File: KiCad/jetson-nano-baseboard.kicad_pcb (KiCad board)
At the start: 8 copper layers, 100.2 x 55 mm, 325 parts, among them IC1 TCA9548ARGER, IC10 TPS62823DLCT, IC11 SN74LV1T125DCKR, IC12 74HC00PW, IC13 SN74LVC1G126DCKR, IC15 TLV70018DCKT, IC16 NCP380HSNAJAAT1G, IC17 AT24CS01-ST, IC3 TPS54561, IC4 TLV70018DCKT, IC6 PCA9517ADP, IC7 HD3SS3220, IC8 LM3671MF-3.3, IC9 LM3671MF-3.3, J1 685119136923, J11 632723300011, J2 2129320-3, J6 WE_68715014522, J7 WE_68715014022, Q1 PMV32UP, T1 BSS138APW, T2 BSS138APW, T3 BSS138APW, T4 BSS138APW, T5 BSS138APW, T6 BSS138APW

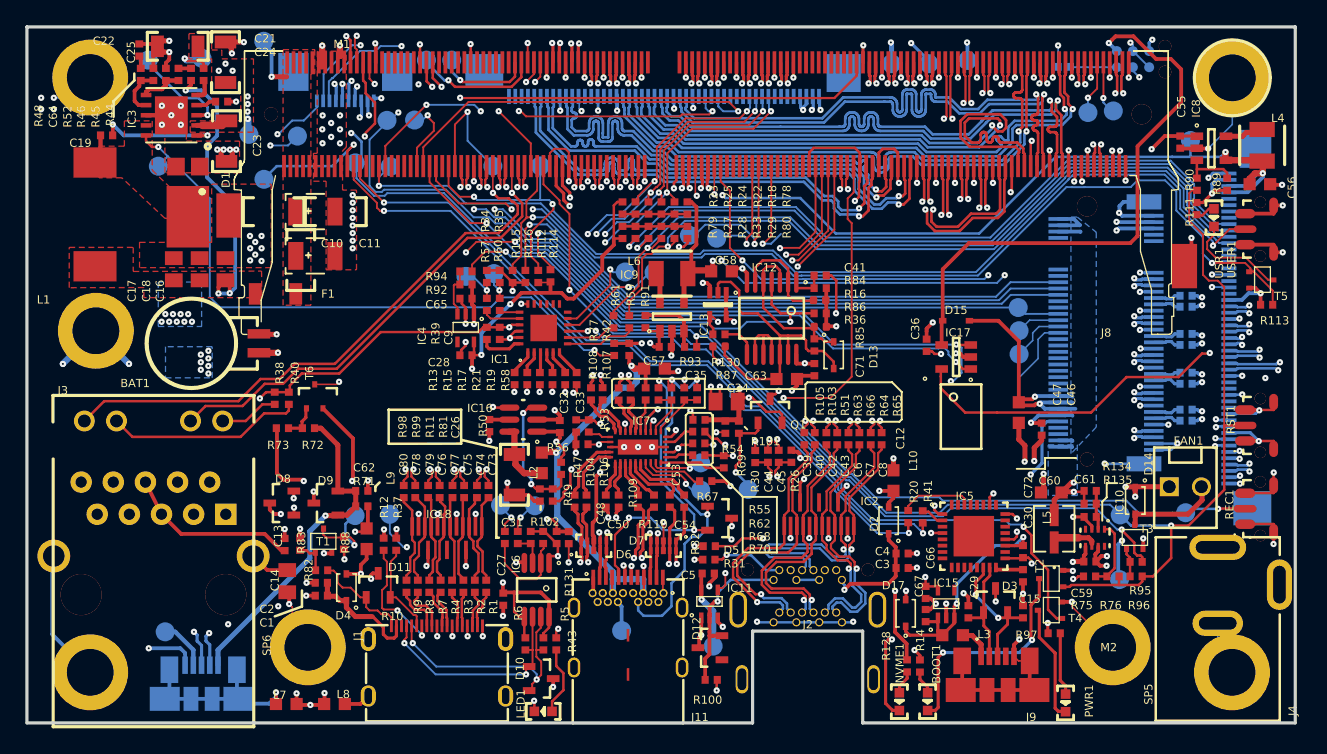
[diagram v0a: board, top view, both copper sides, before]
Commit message: Update 3d models and clean up designators
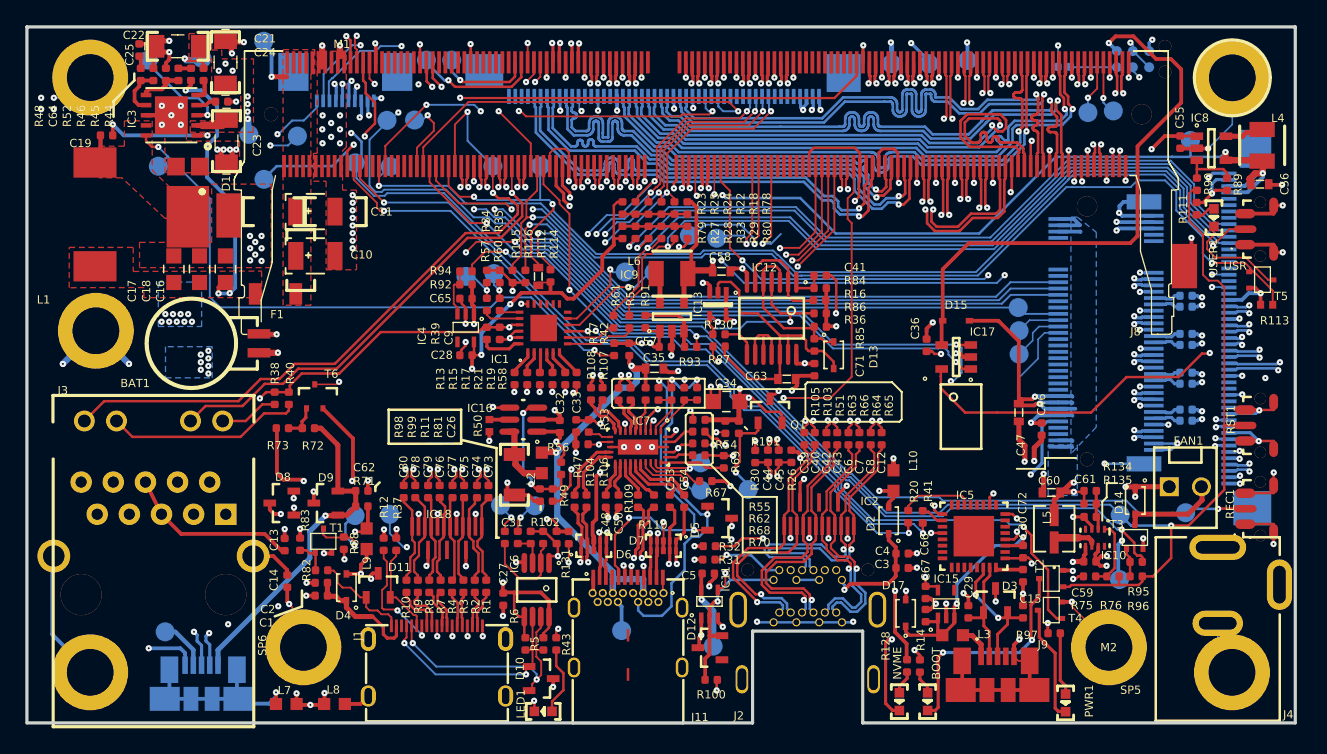
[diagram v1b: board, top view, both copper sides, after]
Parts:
- C1, C2, C3, C4, C62: value 4u7 -> C_4u7_0402; footprint jetson-nano-baseboard-footprints:0402 -> jetson-nano-baseboard-footprints:0402-cap
- C12, C19, C26, C27, C30, C33, C36, C37, C38, C39, C40, C42, C43, C44, C45, C46, C48, C49, C5, C50, C51, C52, C53, C54, C6, C68, C69, C7, C70, C71, C72, C73, C74, C75, C76, C77, C78, C79, C8, C80, C9: value 100n -> C_100n_0402; footprint jetson-nano-baseboard-footprints:0402 -> jetson-nano-baseboard-footprints:0402-cap
- C13, C24: value 10n -> C_10n_0402; footprint jetson-nano-baseboard-footprints:0402 -> jetson-nano-baseboard-footprints:0402-cap
- C14: value 100p -> C_100p_0402; footprint jetson-nano-baseboard-footprints:0805 -> jetson-nano-baseboard-footprints:0402-cap
- C15, C29, C64: value 47p -> C_47p_0402; footprint jetson-nano-baseboard-footprints:0402 -> jetson-nano-baseboard-footprints:0402-cap
- C16, C17, C18, C34: value 47u -> C_47u_0805; footprint jetson-nano-baseboard-footprints:0805 -> jetson-nano-baseboard-footprints:0805-cap
- C21, C22, C23: value 2u2 -> C_2u2_1206; footprint jetson-nano-baseboard-footprints:1206 -> jetson-nano-baseboard-footprints:1206-cap
- C25: value 4n7 -> C_4n7_0402; footprint jetson-nano-baseboard-footprints:0402 -> jetson-nano-baseboard-footprints:0402-cap
- C28, C32, C66: value 1u -> C_1u_0402; footprint jetson-nano-baseboard-footprints:0402 -> jetson-nano-baseboard-footprints:0402-cap
- C35, C47, C56, C58, C60, C63: value 10u -> C_10u_0603; footprint jetson-nano-baseboard-footprints:0603 -> jetson-nano-baseboard-footprints:0603-cap
- C41: value 47n -> C_47n_0402; footprint jetson-nano-baseboard-footprints:0402 -> jetson-nano-baseboard-footprints:0402-cap
- C55, C57: value 4u7 -> C_2u2_0402; footprint jetson-nano-baseboard-footprints:0402 -> jetson-nano-baseboard-footprints:0402-cap
- C59, C65, C67: value 2u2 -> C_2u2_0402; footprint jetson-nano-baseboard-footprints:0402 -> jetson-nano-baseboard-footprints:0402-cap
- C61: value 100p -> C_100p_0402; footprint jetson-nano-baseboard-footprints:0402 -> jetson-nano-baseboard-footprints:0402-cap
- R1, R10, R2, R3, R4, R7, R8, R9: value 5R6 -> R_5R6_0402; footprint jetson-nano-baseboard-footprints:0402 -> jetson-nano-baseboard-footprints:0402-res
- R100, R101, R26, R30, R77: value 100k -> R_100k_0402; footprint jetson-nano-baseboard-footprints:0402 -> jetson-nano-baseboard-footprints:0402-res
- R102, R114, R115, R116, R131, R54, R72, R76, R90, R93, R94, R95, R96: value 10k -> R_10k_0402; footprint jetson-nano-baseboard-footprints:0402 -> jetson-nano-baseboard-footprints:0402-res
- R103, R104, R105, R106, R107, R108, R109, R110, R12, R13, R130, R132, R15, R17, R19, R21, R23, R39, R42, R47, R49, R56, R57, R58, R59, R60, R61, R62, R63, R64, R65, R66, R68, R71, R75, R78, R79, R80, R82, R89, R91, R92, R98, R99: value 0R -> R_0R_0402; footprint jetson-nano-baseboard-footprints:0402 -> jetson-nano-baseboard-footprints:0402-res
- R11, R18, R22, R24, R25, R27, R28, R29, R33, R34, R35, R37, R5, R55, R6, R69, R70, R73, R81, R83, R88: value 2k -> R_2k_0402; footprint jetson-nano-baseboard-footprints:0402 -> jetson-nano-baseboard-footprints:0402-res
- R111, R14, R43, R97: value 470R -> R_470R_0402; footprint jetson-nano-baseboard-footprints:0402 -> jetson-nano-baseboard-footprints:0402-res
- R112: value 100k -> R_110k_0603; footprint jetson-nano-baseboard-footprints:0402 -> jetson-nano-baseboard-footprints:0603-res
- R128, R38, R40: value 220R -> R_220R_0402; footprint jetson-nano-baseboard-footprints:0402 -> jetson-nano-baseboard-footprints:0402-res
- R134, R44: value 243k -> R_243k_0402; footprint jetson-nano-baseboard-footprints:0402 -> jetson-nano-baseboard-footprints:0402-res
- R135, R46: value 53k6 -> R_53k6_0402; footprint jetson-nano-baseboard-footprints:0402 -> jetson-nano-baseboard-footprints:0402-res
- R20, R41: value 22R -> R_22R_0402; footprint jetson-nano-baseboard-footprints:0402 -> jetson-nano-baseboard-footprints:0402-res
- R31, R32: value 1M -> R_1M0_0402; footprint jetson-nano-baseboard-footprints:0402 -> jetson-nano-baseboard-footprints:0402-res
- R45: value 49R9 -> R_49R9_0402; footprint jetson-nano-baseboard-footprints:0402 -> jetson-nano-baseboard-footprints:0402-res
- R48: value 16k9 -> R_16k9_0402; footprint jetson-nano-baseboard-footprints:0402 -> jetson-nano-baseboard-footprints:0402-res
- R51: value 909k -> R_909k_0402; footprint jetson-nano-baseboard-footprints:0402 -> jetson-nano-baseboard-footprints:0402-res
- R52: value 10k2 -> R_10k2_0402; footprint jetson-nano-baseboard-footprints:0402 -> jetson-nano-baseboard-footprints:0402-res
- R53, R67, R84, R86: value 200k -> R_200k_0402; footprint jetson-nano-baseboard-footprints:0402 -> jetson-nano-baseboard-footprints:0402-res
- R85: value 470k -> R_470k_0402; footprint jetson-nano-baseboard-footprints:0402 -> jetson-nano-baseboard-footprints:0402-res
- moved SP6 0.35 mm to (21.8, 48.9)
- moved SP5 0.30 mm to (85.5, 48.9)
- renumbered BOOT1 to BOOT, NVME1 to NVME, USR1 to USR
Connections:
- R50 pad 1: GND -> Net-(R50-Pad1)
- R50 pad 2: Net-(IC16-Pad5) -> Net-(R50-Pad2)
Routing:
- net Net-(R50-Pad1): track 0.00 -> 0.50 mm, vias 0 -> 1
- net GND: track 410.6 -> 410.5 mm, vias 228 -> 227
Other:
- board text removed: "C10"
- board text removed: "C11"
- board text removed: "C12"
- board text removed: "C13"
- board text removed: "C20"
- board text removed: "C22"
- board text removed: "C25"
- board text removed: "C26"
- board text removed: "C27"
- board text removed: "C28"
- board text removed: "C29"
- board text removed: "C30"
- board text removed: "C32"
- board text removed: "C33"
- board text removed: "C34"
- board text removed: "C35"
- board text removed: "C39"
- board text removed: "C40"
- board text removed: "C42"
- board text removed: "C43"
- board text removed: "C44"
- board text removed: "C45"
- board text removed: "C46"
- board text removed: "C47"
- board text removed: "C48"
- board text removed: "C50"
- board text removed: "C53"
- board text removed: "C54"
- board text removed: "C55"
- board text removed: "C56"
- board text removed: "C57"
- board text removed: "C58"
- board text removed: "C6"
- board text removed: "C65"
- board text removed: "C66"
- board text removed: "C67"
- board text removed: "C7"
- board text removed: "C72"
- board text removed: "C73"
- board text removed: "C74"
- board text removed: "C75"
- board text removed: "C76"
- board text removed: "C77"
- board text removed: "C78"
- board text removed: "C79"
- board text removed: "C8"
- board text removed: "C80"
- board text removed: "D1"
- board text removed: "D12"
- board text removed: "D14"
- board text removed: "D2"
- board text removed: "D5"
- board text removed: "F1"
- board text removed: "IC10"
- board text removed: "IC11"
- board text removed: "IC13"
- board text removed: "IC14"
- board text removed: "IC15"
- board text removed: "IC17"
- board text removed: "IC5"
- board text removed: "IC8"
- board text removed: "J9"
- board text removed: "L2"
- board text removed: "L9"
- board text removed: "NVME"
- board text removed: "Q2"
- board text removed: "R1"
- board text removed: "R10"
- board text removed: "R100"
- board text removed: "R103"
- board text removed: "R105"
- board text removed: "R107"
- board text removed: "R108"
- board text removed: "R109"
- board text removed: "R11"
- board text removed: "R111"
- board text removed: "R117"
- board text removed: "R118"
- board text removed: "R119"
- board text removed: "R120"
- board text removed: "R121"
- board text removed: "R122"
- board text removed: "R123"
- board text removed: "R124"
- board text removed: "R125"
- board text removed: "R126"
- board text removed: "R127"
- board text removed: "R129"
- board text removed: "R13"
- board text removed: "R130"
- board text removed: "R131"
- board text removed: "R15"
- board text removed: "R17"
- board text removed: "R18"
- board text removed: "R19"
- board text removed: "R2"
- board text removed: "R21"
- board text removed: "R22"
- board text removed: "R23"
- board text removed: "R24"
- board text removed: "R25"
- board text removed: "R26"
- board text removed: "R27"
- board text removed: "R28"
- board text removed: "R29"
- board text removed: "R3"
- board text removed: "R30"
- board text removed: "R31"
- board text removed: "R32"
- board text removed: "R33"
- board text removed: "R38"
- board text removed: "R4"
- board text removed: "R40"
- board text removed: "R42"
- board text removed: "R43"
- board text removed: "R5"
- board text removed: "R50"
- board text removed: "R51"
- board text removed: "R54"
- board text removed: "R55"
- board text removed: "R58"
- board text removed: "R6"
- board text removed: "R62"
- board text removed: "R63"
- board text removed: "R64"
- board text removed: "R65"
- board text removed: "R66"
- board text removed: "R67"
- board text removed: "R68"
- board text removed: "R69"
- board text removed: "R7"
- board text removed: "R70"
- board text removed: "R74"
- board text removed: "R77"
- board text removed: "R78"
- board text removed: "R79"
- board text removed: "R8"
- board text removed: "R80"
- board text removed: "R81"
- board text removed: "R82"
- board text removed: "R83"
- board text removed: "R87"
- board text removed: "R88"
- board text removed: "R89"
- board text removed: "R9"
- board text removed: "R90"
- board text removed: "R92"
- board text removed: "R94"
- board text removed: "R95"
- board text removed: "R98"
- board text removed: "R99"
- board text removed: "SP5"
- board text removed: "T1"
- board text removed: "T3"
- board text removed: "USER"

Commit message: Fix DRC errors
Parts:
- moved C25 0.29 mm to (8.54, 1.73)
- moved D1 0.13 mm to (12.6, 14.3)
- renumbered BOOT to BOOT1, NVME to NVME1, USR to USR1
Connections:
- R50 pad 1: Net-(R50-Pad1) -> GND
- R50 pad 2: Net-(R50-Pad2) -> Net-(IC16-Pad5)
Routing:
- net GND: track 410.5 -> 411.3 mm, vias 227 -> 228
- net Net-(R50-Pad1): track 0.50 -> 0.00 mm, vias 1 -> 0
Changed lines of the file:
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@@
     (zones 0)
     (modules 325)
-    (nets 441)
+    (nets 439)
   )
   (page A4)
   (layers
     (0 F.Cu signal)
-    (1 In1.Cu signal)
-    (2 In2.Cu signal)
-    (3 In3.Cu signal)
-    (4 In4.Cu signal)
-    (5 In5.Cu signal)
-    (6 In6.Cu signal)
+    (1 In1.Cu signal hide)
+    (2 In2.Cu signal hide)
+    (3 In3.Cu signal hide)
+    (4 In4.Cu signal hide)
+    (5 In5.Cu signal hide)
+    (6 In6.Cu signal hide)
     (31 B.Cu signal)
     (32 B.Adhes user hide)
     (33 F.Adhes user hide)
-    (34 B.Paste user hide)
-    (35 F.Paste user hide)
-    (36 B.SilkS user hide)
-    (37 F.SilkS user hide)
+    (34 B.Paste user)
+    (35 F.Paste user)
+    (36 B.SilkS user)
+    (37 F.SilkS user)
     (38 B.Mask user hide)
     (39 F.Mask user hide)
-    (40 Dwgs.User user)
+    (40 Dwgs.User user hide)
     (41 Cmts.User user hide)
     (42 Eco1.User user hide)
@@
     (45 Margin user hide)
     (46 B.CrtYd user hide)
-    (47 F.CrtYd user hide)
+    (47 F.CrtYd user)
     (48 B.Fab user hide)
     (49 F.Fab user hide)
@@
   (net 437 PWR_GOOD)
   (net 438 "#RECOVERY")
-  (net 439 "Net-(R50-Pad1)")
-  (net 440 "Net-(R50-Pad2)")
   (net_class Default "This is the default net class."
     (clearance 0.1)
@@
     (add_net "Net-(R27-Pad1)")
     (add_net "Net-(R45-Pad1)")
-    (add_net "Net-(R50-Pad1)")
-    (add_net "Net-(R50-Pad2)")
     (add_net "Net-(R72-Pad2)")
     (add_net "Net-(R82-Pad2)")
@@
   )
   (module jetson-nano-baseboard-footprints:0402-res (layer F.Cu)
-    (at 85.7822 43.32361)
+    (at 85.745 43.32)
     (descr "Resistor SMD 0402 (1005 Metric), square (rectangular) end terminal, IPC_7351 nominal, (Body size source: http://www.tortai-tech.com/upload/download/2011102023233369053.pdf), generated with kicad-footprint-generator")
     (tags resistor)
@@
   )
   (module jetson-nano-baseboard-footprints:0402-res (layer F.Cu)
-    (at 83.928 43.32361 180)
+    (at 83.88 43.32 180)
     (descr "Resistor SMD 0402 (1005 Metric), square (rectangular) end terminal, IPC_7351 nominal, (Body size source: http://www.tortai-tech.com/upload/download/2011102023233369053.pdf), generated with kicad-footprint-generator")
     (tags resistor)
@@
   )
   (module jetson-nano-baseboard-footprints:0402-cap (layer F.Cu)
-    (at 8.83927 1.7324 270)
+    (at 8.545 1.725 270)
     (descr "Resistor SMD 0402 (1005 Metric), square (rectangular) end terminal, IPC_7351 nominal, (Body size source: http://www.tortai-tech.com/upload/download/2011102023233369053.pdf), generated with kicad-footprint-generator")
     (tags resistor)
     (attr smd)
-    (fp_text reference C25 (at 0.3676 0.76927 90) (layer F.SilkS)
+    (fp_text reference C25 (at 0.3 0.84 90) (layer F.SilkS)
       (effects (font (size 0.65 0.65) (thickness 0.15)))
     )
@@
     (at 97.424 15.88801)
     (attr smd)
-    (fp_text reference USR (at -1.979 2.89699) (layer F.SilkS)
+    (fp_text reference USR1 (at -1.979 2.89699) (layer F.SilkS)
       (effects (font (size 0.65 0.65) (thickness 0.15)))
     )
@@
     )
     (pad 1 smd rect (at -0.48 0 180) (size 0.62 0.57) (layers F.Cu F.Paste F.Mask)
-      (net 439 "Net-(R50-Pad1)"))
+      (net 6 GND))
     (pad 2 smd rect (at 0.48 0 180) (size 0.62 0.57) (layers F.Cu F.Paste F.Mask)
-      (net 440 "Net-(R50-Pad2)"))
+      (net 84 "Net-(IC16-Pad5)"))
     (model ${KIPRJMOD}/nano-baseboard-3dmodels/0402-res.step
       (at (xyz 0 0 0))
@@
     (at 68.89971 53.2221 90)
     (attr smd)
-    (fp_text reference NVME (at 3.0371 -0.15471 270) (layer F.SilkS)
+    (fp_text reference NVME1 (at 3.0371 -0.15471 270) (layer F.SilkS)
       (effects (font (size 0.65 0.65) (thickness 0.15)))
     )
@@
   )
   (module jetson-nano-baseboard-footprints:PowerDI (layer F.Cu)
-    (at 12.5794 14.40601 90)
+    (at 12.58 14.275 90)
     (attr smd)
     (fp_text reference D1 (at 2.12601 3.1206 90) (layer F.SilkS)
@@
     (at 71.13348 53.2221 90)
     (attr smd)
-    (fp_text reference BOOT (at 3.0171 0.68152 270) (layer F.SilkS)
+    (fp_text reference BOOT1 (at 3.0171 0.68152 270) (layer F.SilkS)
       (effects (font (size 0.65 0.65) (thickness 0.15)))
     )
@@
   (segment (start 47.277 12.10581) (end 47.277 10.90601) (width 0.25) (layer F.Cu) (net 6))
   (segment (start 45.777 12.10581) (end 45.777 10.90601) (width 0.25) (layer F.Cu) (net 6))
-  (segment (start 36.49742 32.61514) (end 36.49742 32.11879) (width 0.3) (layer F.Cu) (net 439))
+  (segment (start 36.49742 32.61514) (end 36.49742 32.11879) (width 0.3) (layer F.Cu) (net 6))
   (segment (start 30.90199 39.38102) (end 30.90199 38.40204) (width 0.2) (layer F.Cu) (net 6))
   (segment (start 30.90199 38.40204) (end 30.91747 38.38656) (width 0.2) (layer F.Cu) (net 6))
@@
   (segment (start 10.73355 1.89621) (end 11.2078 1.89621) (width 0.4) (layer F.Cu) (net 6))
   (segment (start 10.27464 1.4373) (end 10.73355 1.89621) (width 0.4) (layer F.Cu) (net 6))
-  (segment (start 8.83927 1.2524) (end 10.08974 1.2524) (width 0.3) (layer F.Cu) (net 6))
-  (segment (start 10.08974 1.2524) (end 10.27464 1.4373) (width 0.3) (layer F.Cu) (net 6))
   (segment (start 9.94894 3.18058) (end 9.94894 1.763) (width 0.3) (layer F.Cu) (net 6))
   (segment (start 9.94894 1.763) (end 10.27464 1.4373) (width 0.3) (layer F.Cu) (net 6))
@@
   (via (at 59.02579 3.90701) (size 0.5) (drill 0.15) (layers F.Cu B.Cu) (net 6))
   (via (at 60.52579 3.90701) (size 0.5) (drill 0.15) (layers F.Cu B.Cu) (net 6))
-  (via (at 36.49742 32.61514) (size 0.5) (drill 0.15) (layers F.Cu B.Cu) (net 439))
+  (via (at 36.49742 32.61514) (size 0.5) (drill 0.15) (layers F.Cu B.Cu) (net 6))
   (via (at 30.91747 38.38656) (size 0.5) (drill 0.15) (layers F.Cu B.Cu) (net 6))
   (via (at 32.41747 38.38656) (size 0.5) (drill 0.15) (layers F.Cu B.Cu) (net 6))
@@
   (segment (start 20.5296 44.18961) (end 20.53 44.19001) (width 0.3) (layer F.Cu) (net 6))
   (segment (start 20.53 44.19001) (end 20.53 45.35601) (width 0.3) (layer F.Cu) (net 6))
+  (segment (start 10.07734 1.24) (end 10.27464 1.4373) (width 0.3) (layer F.Cu) (net 6))
+  (segment (start 8.545 1.24) (end 10.07734 1.24) (width 0.3) (layer F.Cu) (net 6))
   (segment (start 26.8542 41.34461) (end 27.032 41.16681) (width 0.3) (layer F.Cu) (net 7))
   (segment (start 26.8034 41.95201) (end 26.8034 41.16681) (width 0.3) (layer F.Cu) (net 7))
@@
   (segment (start 14.1052 6.08541) (end 14.3828 5.80781) (width 0.3) (layer F.Cu) (net 19))
   (segment (start 14.3828 5.80781) (end 14.868 5.80781) (width 0.3) (layer F.Cu) (net 19))
-  (segment (start 8.95683 3.18139) (end 8.95683 2.32996) (width 0.3) (layer F.Cu) (net 20))
-  (segment (start 8.83927 2.2124) (end 8.95683 2.32996) (width 0.3) (layer F.Cu) (net 20))
+  (segment (start 8.95683 2.62183) (end 8.95683 3.18139) (width 0.3) (layer F.Cu) (net 20))
+  (segment (start 8.545 2.21) (end 8.95683 2.62183) (width 0.3) (layer F.Cu) (net 20))
   (segment (start 76.534 42.79281) (end 76.534 42.62361) (width 0.3) (layer F.Cu) (net 21))
   (segment (start 76.534 42.79281) (end 78.6702 42.79281) (width 0.3) (layer F.Cu) (net 21))
